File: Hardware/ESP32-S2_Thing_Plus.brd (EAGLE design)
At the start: 22.9 x 64.8 mm, 124 parts, among them J3 QWIIC_RA, J5 USB-C, J6 JTAG, Q1 2.5A/30V, Q2 MBT3904DW1T1, U1 MCP73831, U2 ESP32-S2-WROOM, U3 AP2112K-3.3V, U4 CP210X, Y1 32.768kHz

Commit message: routing "done"
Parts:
- removed J1: (no value), SparkFun-Connectors:2X3_SMT_POSTS
- removed LOGO5: SFE_LOGO_NAME_FLAME.1_INCH, SparkFun-Aesthetics:SFE_LOGO_NAME_FLAME_.1
- removed U$27: (no value), output:#A1#0
- removed U$68: (no value), output:320
- removed U$69: (no value), output:150
- removed U$70: (no value), output:330
- removed U$71: (no value), output:270
- removed U$93: (no value), output:160
- removed U$94: (no value), output:170
- removed U$95: (no value), output:210
- added J7: (no value), SparkFun-Connectors:2X4_SMT_NO_POSTS_NS
- added LOGO1: SFE_LOGO_FLAME.1_INCH, SparkFun-Aesthetics:SFE_LOGO_FLAME_.1
- added U$15: (no value), output:110
- added U$17: (no value), output:100
- added U$18: (no value), output:80
- added U$20: (no value), output:60
- added U$23: (no value), output:40
- added U$24: (no value), output:330
- added U$29: (no value), output:340
- added U$30: (no value), output:30
- added U$47: (no value), output:#11#0
- added U$48: (no value), output:#6#0
- added U$49: (no value), output:#8#0
- added U$50: (no value), output:#10#0
- added U$51: (no value), output:#4#0
- added U$52: (no value), output:#1#SDA#0
- added U$53: (no value), output:#2#SCL#0
- added U$54: (no value), output:#21#0
- added U$55: (no value), output:#26#0
- added U$56: (no value), output:#TX0#0
- added U$57: (no value), output:#38#0
- added U$60: (no value), output:#100#0
- added U$61: (no value), output:THING_PLUS0
- added U$62: (no value), output:THING_PLUS_0
- added U$63: (no value), output:ESP32#S2_0
- added U$64: (no value), output:#A1#0
- U$10: device output:#18#COPI#0 -> output:#45#0
- U$11: device output:#5#SCK#0 -> output:MA0
- U$21: device output:#A3#0 -> output:#A2#0
- U$22: device output:#A2#0 -> output:#A3#0
- U$3: device output:#21#0 -> output:CHG0
- U$31: device output:#23#SDA#0 -> output:#36#SCK#0
- U$33: device output:#22#SCL#0 -> output:#35#COPI#0
- U$34: device output:#14#0 -> output:#37#CIPO#0
- U$35: device output:#32#0 -> output:#33#RX1#0
- U$36: device output:#15#0 -> output:#34#TX1#0
- U$37: device output:#33#0 -> output:#3#0
- U$38: device output:#27#0 -> output:#41#MTDI#0
- U$4: device output:#17#TX1#0 -> output:#500#0
- U$5: device output:#16#RX1#0 -> output:ESP32#S20
- U$58: device output:140 -> output:#RX0#0
- U$8: device output:#19#CIPO#0 -> output:#46#0
- moved LOGO2 71.4 mm to (11.4, 3.81), flipped to the bottom
- moved LOGO3 44.3 mm to (11.6, 60.1)
- moved U$4 33.2 mm to (9.03, 23.7), turned to 90 degrees
- moved U$31 31.2 mm to (21.4, 39.4)
- moved U$3 31.1 mm to (12.0, 25.1), turned to 90 degrees
- moved U$33 29.5 mm to (21.4, 41.9)
- moved U$37 27.8 mm to (21.4, 52.1)
- moved U$36 25.8 mm to (21.4, 49.5)
- moved U$35 24.8 mm to (21.4, 47.0)
- moved U$34 24.8 mm to (21.4, 44.5)
- moved U$5 21.5 mm to (11.3, 57.7)
- moved U$9 19.7 mm to (50.0, 54.9), flipped to the bottom
- moved U$38 18.3 mm to (12.7, 45.6), turned to 90 degrees
- moved U$11 17.5 mm to (10.9, 25.2), turned to 90 degrees
- moved U$8 16.1 mm to (5.07, 45.6), turned to 90 degrees
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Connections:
- net 33 renamed 33/RX1
- net 34 renamed 34/TX1
- removed net MTDI: J6.8, U2.35
- removed net N$14: J1.2
- removed net N$15: J1.4
- removed net N$16: J1.6
- removed net N$18: J1.1
- removed net N$19: J1.3
- removed net N$20: J1.5
- removed net RX: U2.37, U4.20
- removed net TX: U2.38, U4.21
- new net 41/MTDI: J6.8, J7.7, U2.35
- new net RX0: J7.5, U2.38, U4.21
- new net TX0: J7.6, U2.37, U4.20
- net 21: now also J7.2
- net 26: now also J7.4
- net 38: now also J7.8
- net 45: now also J7.3
- net 46: now also J7.1
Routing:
- net TX0: track 0.00 -> 49.8 mm, vias 0 -> 3
- net RX0: track 0.00 -> 47.5 mm, vias 0 -> 3
- net TX: track 37.1 -> 0.00 mm, vias 2 -> 0
- net RX: track 35.4 -> 0.00 mm, vias 2 -> 0
- net 41/MTDI: track 0.00 -> 26.2 mm, vias 0 -> 1
- net 46: track 0.00 -> 23.4 mm, vias 0 -> 1
- net MTDI: track 22.1 -> 0.00 mm, vias 1 -> 0
- net 45: track 0.00 -> 22.0 mm, vias 0 -> 1
- net 21: track 0.00 -> 15.2 mm, vias 0 -> 1
- net 26: track 0.00 -> 14.5 mm, vias 0 -> 1
- net 38: track 0.00 -> 9.15 mm, vias 0 -> 1
- net A5: track 23.0 -> 24.9 mm
- net 34/TX1: track 23.7 -> 25.4 mm
- net A2: track 32.9 -> 34.0 mm

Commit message: DRC errors  - some little nudging
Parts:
- removed U$9: (no value), output:ESP32#S2_THING_PLUS0
- moved FD3 0.08 mm to (0.74, 3.63)
- moved FD4 0.08 mm to (0.74, 3.63)
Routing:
- net GND: track 3.46 -> 2.38 mm

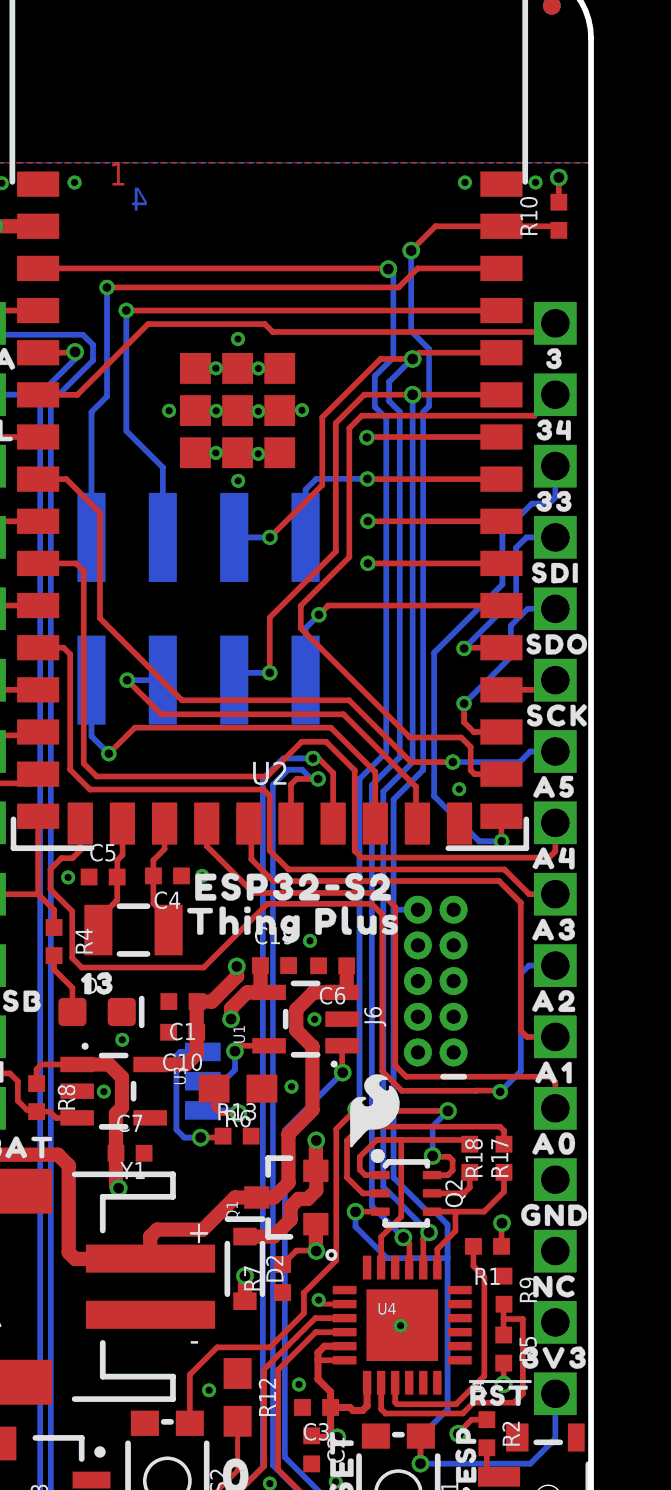
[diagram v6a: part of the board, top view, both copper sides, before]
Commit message: schematic cleanup and added recommended RC (cap to GND) on enable pin
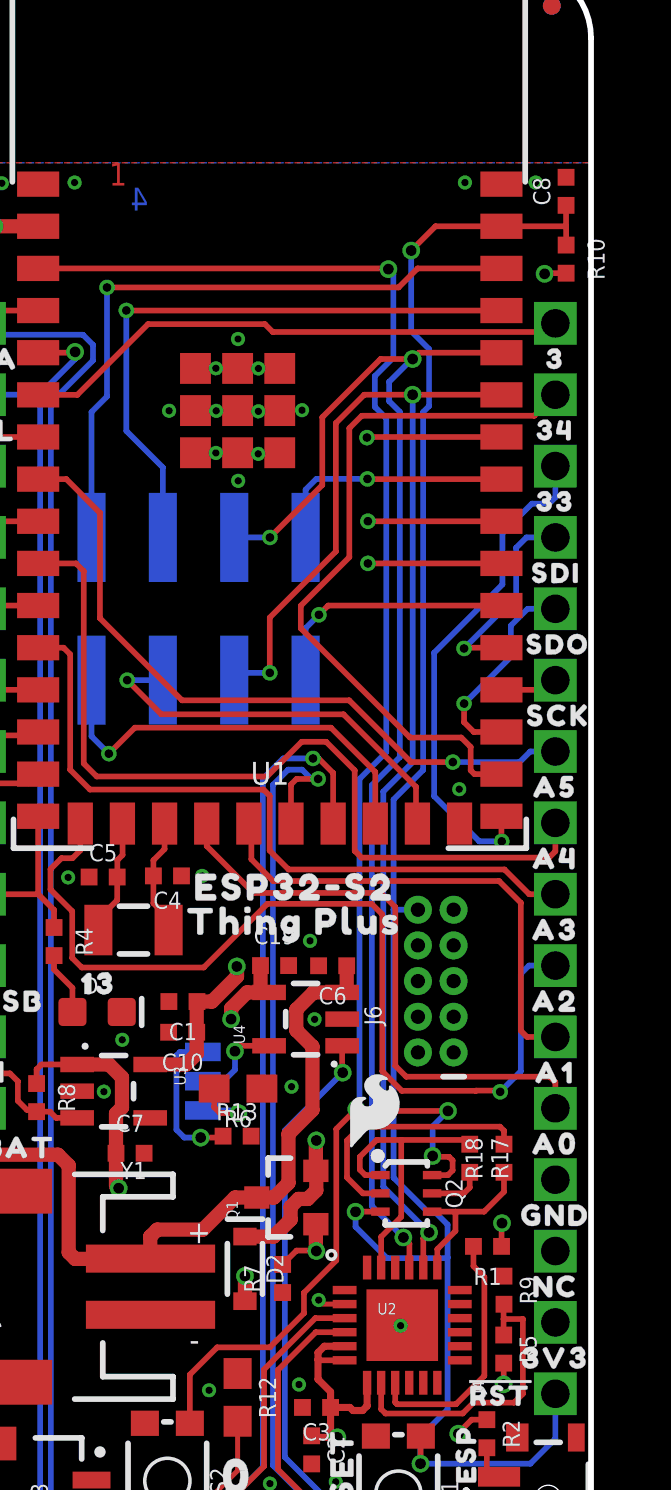
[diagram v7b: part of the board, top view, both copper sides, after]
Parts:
- added C8: 0.1uF, SparkFun-Capacitors:0402-TIGHT
- U1: value MCP73831 -> ESP32-S2-WROOM; device SparkFun-PowerIC:SOT23-5 -> esp32-s2-wroom:ESP32-S2-WROOM
- U2: value ESP32-S2-WROOM -> CP210X; device esp32-s2-wroom:ESP32-S2-WROOM -> SparkFun-IC-Comms:QFN24
- U4: value CP210X -> MCP73831; device SparkFun-IC-Comms:QFN24 -> SparkFun-PowerIC:SOT23-5
- moved U2 29.1 mm to (16.1, 16.4), turned to 0 degrees
- moved U1 17.8 mm to (11.4, 45.1)
- moved U4 11.4 mm to (12.7, 27.3), turned to 90 degrees
- moved R10 1.55 mm to (22.0, 54.4), turned to 270 degrees
- renumbered U$13 to U5
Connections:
- net 0: now also U1.3; no longer U2.3
- net 10: now also U1.13; no longer U2.13
- net 11: now also U1.14; no longer U2.14
- net 12: now also U1.15; no longer U2.15
- net 13: now also U1.16; no longer U2.16
- net 21: now also U1.24; no longer U2.24
- net 26: now also U1.25; no longer U2.25
- net 3: now also U1.6; no longer U2.6
- net 3.3V: now also U1.2, U2.5, U2.6, U2.7; no longer U2.2, U4.5, U4.6, U4.7
- net 33/RX1: now also U1.27; no longer U2.27
- net 34/TX1: now also U1.28; no longer U2.28
- net 38: now also U1.32; no longer U2.32
- net 4: now also U1.7; no longer U2.7
- net 41/MTDI: now also U1.35; no longer U2.35
- net 45: now also U1.39; no longer U2.39
- net 46: now also U1.40; no longer U2.40
- net 6: now also U1.9; no longer U2.9
- net 8: now also U1.11; no longer U2.11
- net A0: now also U1.20; no longer U2.20
- net A1: now also U1.21; no longer U2.21
- net A2: now also U1.17; no longer U2.17
- net A3: now also U1.12; no longer U2.12
- net A4: now also U1.10; no longer U2.10
- net A5: now also U1.8; no longer U2.8
- net CHG: now also U4.1; no longer U1.1
- net CHIP_PU: now also C8.1, U1.41; no longer U2.41
- net CIPO: now also U1.31; no longer U2.31
- net COPI: now also U1.29; no longer U2.29
- net CP210X_D+: now also U2.3; no longer U4.3
- net CP210X_D-: now also U2.4; no longer U4.4
- net DTR: now also U2.23; no longer U4.23
- net ESP32_D+: now also U1.23; no longer U2.23
- net ESP32_D-: now also U1.22; no longer U2.22
- net GND: now also C8.2, U1.1, U1.26, U1.42, U1.GNDEP0, U1.GNDEP1, U1.GNDEP2, U1.GNDEP3, U1.GNDEP4, U1.GNDEP5, U1.GNDEP6, U1.GNDEP7, U1.GNDEP8, U2.2, U2.PAD; no longer U1.2, U2.1, U2.26, U2.42, U2.GNDEP0, U2.GNDEP1, U2.GNDEP2, U2.GNDEP3, U2.GNDEP4, U2.GNDEP5, U2.GNDEP6, U2.GNDEP7, U2.GNDEP8, U4.PAD
- net MTCK: now also U1.33; no longer U2.33
- net MTDO: now also U1.34; no longer U2.34
- net MTMS: now also U1.36; no longer U2.36
- net N$1: now also U2.9; no longer U4.9
- net N$4: now also U2.8; no longer U4.8
- net N$7: now also U1.18; no longer U2.18
- net N$8: now also U1.19; no longer U2.19
- net N$9: now also U4.5; no longer U1.5
- net RTS: now also U2.19; no longer U4.19
- net RX0: now also U1.38, U2.21; no longer U2.38, U4.21
- net SCK: now also U1.30; no longer U2.30
- net SCL: now also U1.5; no longer U2.5
- net SDA: now also U1.4; no longer U2.4
- net TX0: now also U1.37, U2.20; no longer U2.37, U4.20
- net V_BATT: now also U4.3; no longer U1.3
- net V_USB: now also U4.4; no longer U1.4
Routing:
- net CHIP_PU: track 64.8 -> 66.4 mm

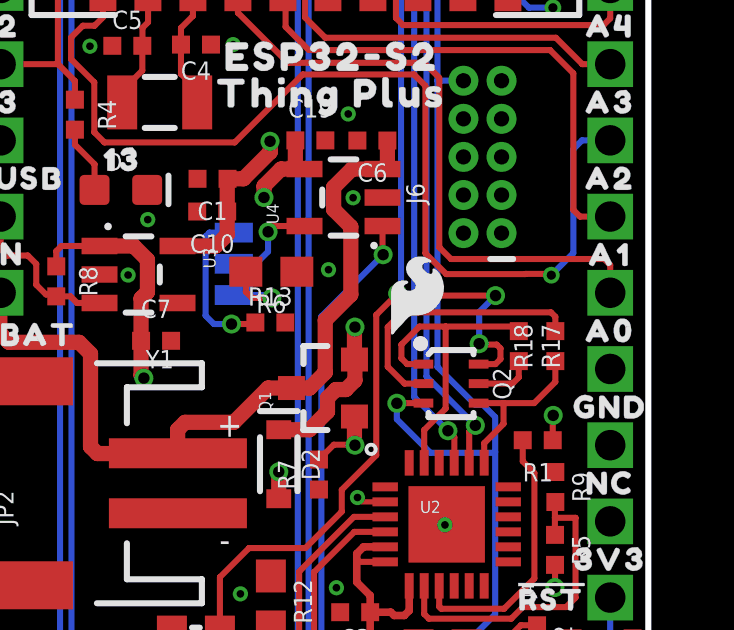
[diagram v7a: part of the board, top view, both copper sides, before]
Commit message: "0" boot test point moved to 50 mil grid
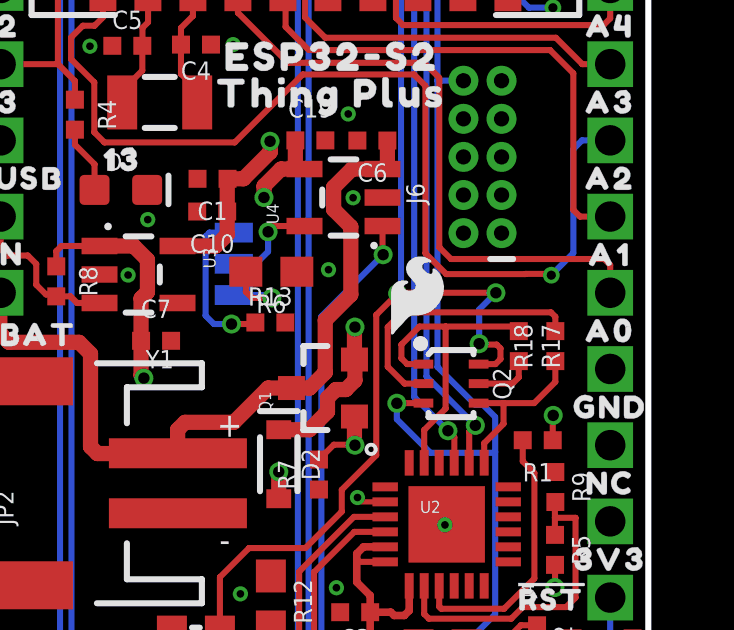
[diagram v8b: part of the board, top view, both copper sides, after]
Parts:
- moved TP1 0.09 mm to (17.8, 24.1)
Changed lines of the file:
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@@
 <layers>
 <layer number="1" name="Top" color="4" fill="1" visible="yes" active="yes"/>
-<layer number="2" name="Route2" color="1" fill="3" visible="no" active="yes"/>
-<layer number="15" name="Route15" color="4" fill="6" visible="no" active="yes"/>
+<layer number="2" name="Route2" color="1" fill="3" visible="yes" active="yes"/>
+<layer number="15" name="Route15" color="4" fill="6" visible="yes" active="yes"/>
 <layer number="16" name="Bottom" color="1" fill="1" visible="yes" active="yes"/>
 <layer number="17" name="Pads" color="2" fill="1" visible="yes" active="yes"/>
@@
 <attribute name="VALUE" x="6.25601875" y="10.868659375" size="0.6096" layer="27" font="vector" ratio="20" rot="R270" align="top-center"/>
 </element>
-<element name="TP1" library="SparkFun-Connectors" package="TP_15TH" value="" x="17.7673" y="24.036021875" smashed="yes"/>
+<element name="TP1" library="SparkFun-Connectors" package="TP_15TH" value="" x="17.78" y="24.13" smashed="yes"/>
 <element name="J5" library="SparkFun-Connectors" package="USB-C-16P-4LAYER-ISOLATED" value="USB-C" x="11.43" y="6.604" smashed="yes">
 <attribute name="NAME" x="10.414" y="1.905" size="0.508" layer="25" font="vector"/>
@@
 <wire x1="17.2513" y1="22.4028" x2="17.2212" y2="22.4329" width="0.2032" layer="1"/>
 <via x="17.2212" y="22.4329" extent="1-16" drill="0.381"/>
-<wire x1="17.2212" y1="22.4329" x2="17.2212" y2="23.489921875" width="0.2032" layer="16"/>
-<wire x1="17.2212" y1="23.489921875" x2="17.7673" y2="24.036021875" width="0.2032" layer="16"/>
+<wire x1="17.2212" y1="22.4329" x2="17.2212" y2="23.5712" width="0.2032" layer="16"/>
+<wire x1="17.2212" y1="23.5712" x2="17.78" y2="24.13" width="0.2032" layer="16"/>
 <wire x1="17.764521875" y1="21.752321875" x2="17.9324" y2="21.9202" width="0.2032" layer="1"/>
 <wire x1="17.9324" y1="21.9202" x2="17.9324" y2="22.2758" width="0.2032" layer="1"/>
@@
 <wire x1="12.64158125" y1="17.564103125" x2="12.64158125" y2="16.83511875" width="0.2032" layer="1"/>
 <wire x1="12.64158125" y1="16.83511875" x2="11.4274625" y2="15.621" width="0.2032" layer="1"/>
-<wire x1="17.7673" y1="24.036021875" x2="14.571978125" y2="24.036021875" width="0.2032" layer="1"/>
-<wire x1="14.5034" y1="24.1046" x2="14.571978125" y2="24.036021875" width="0.2032" layer="1"/>
+<wire x1="14.5034" y1="24.1046" x2="14.5288" y2="24.13" width="0.2032" layer="1"/>
+<wire x1="17.78" y1="24.13" x2="14.5288" y2="24.13" width="0.2032" layer="1"/>
 <via x="14.5034" y="24.1046" extent="1-16" drill="0.381"/>
 <wire x1="14.5034" y1="24.1046" x2="14.6177" y2="24.2189" width="0.2032" layer="16"/>
